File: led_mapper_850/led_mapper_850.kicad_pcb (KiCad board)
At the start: 2 copper layers, 530 parts, among them J1 Conn_02x12_Top_Bottom

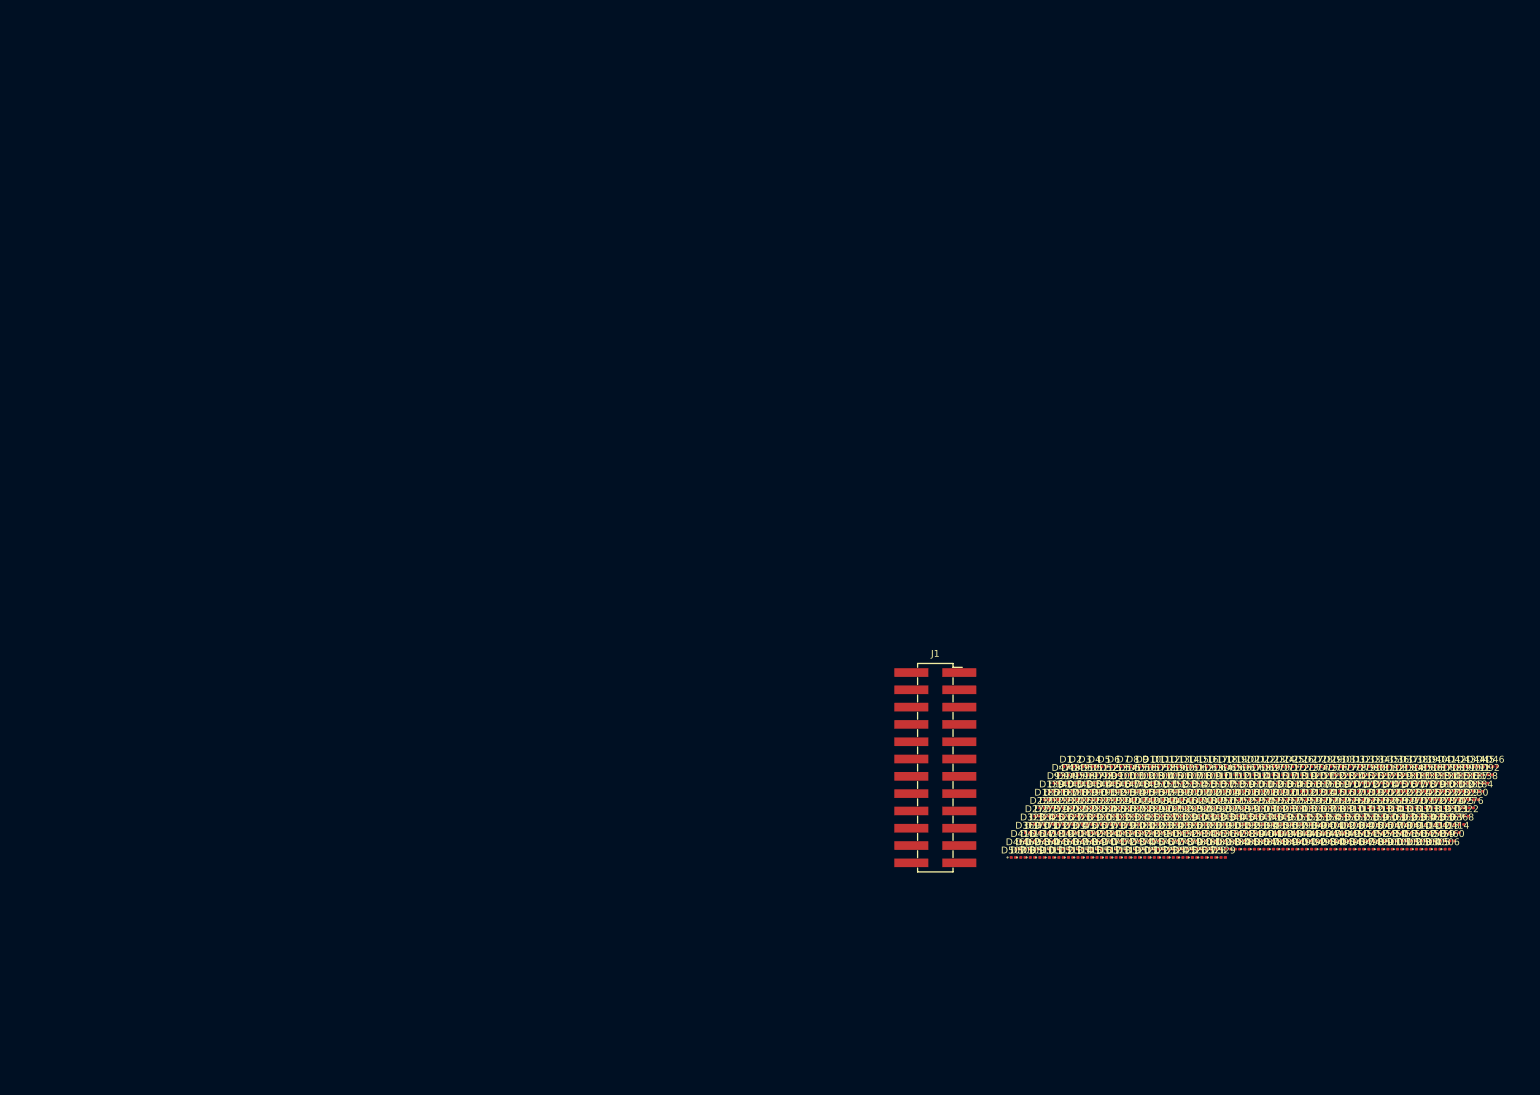
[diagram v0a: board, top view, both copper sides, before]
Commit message: update pcb from schematic
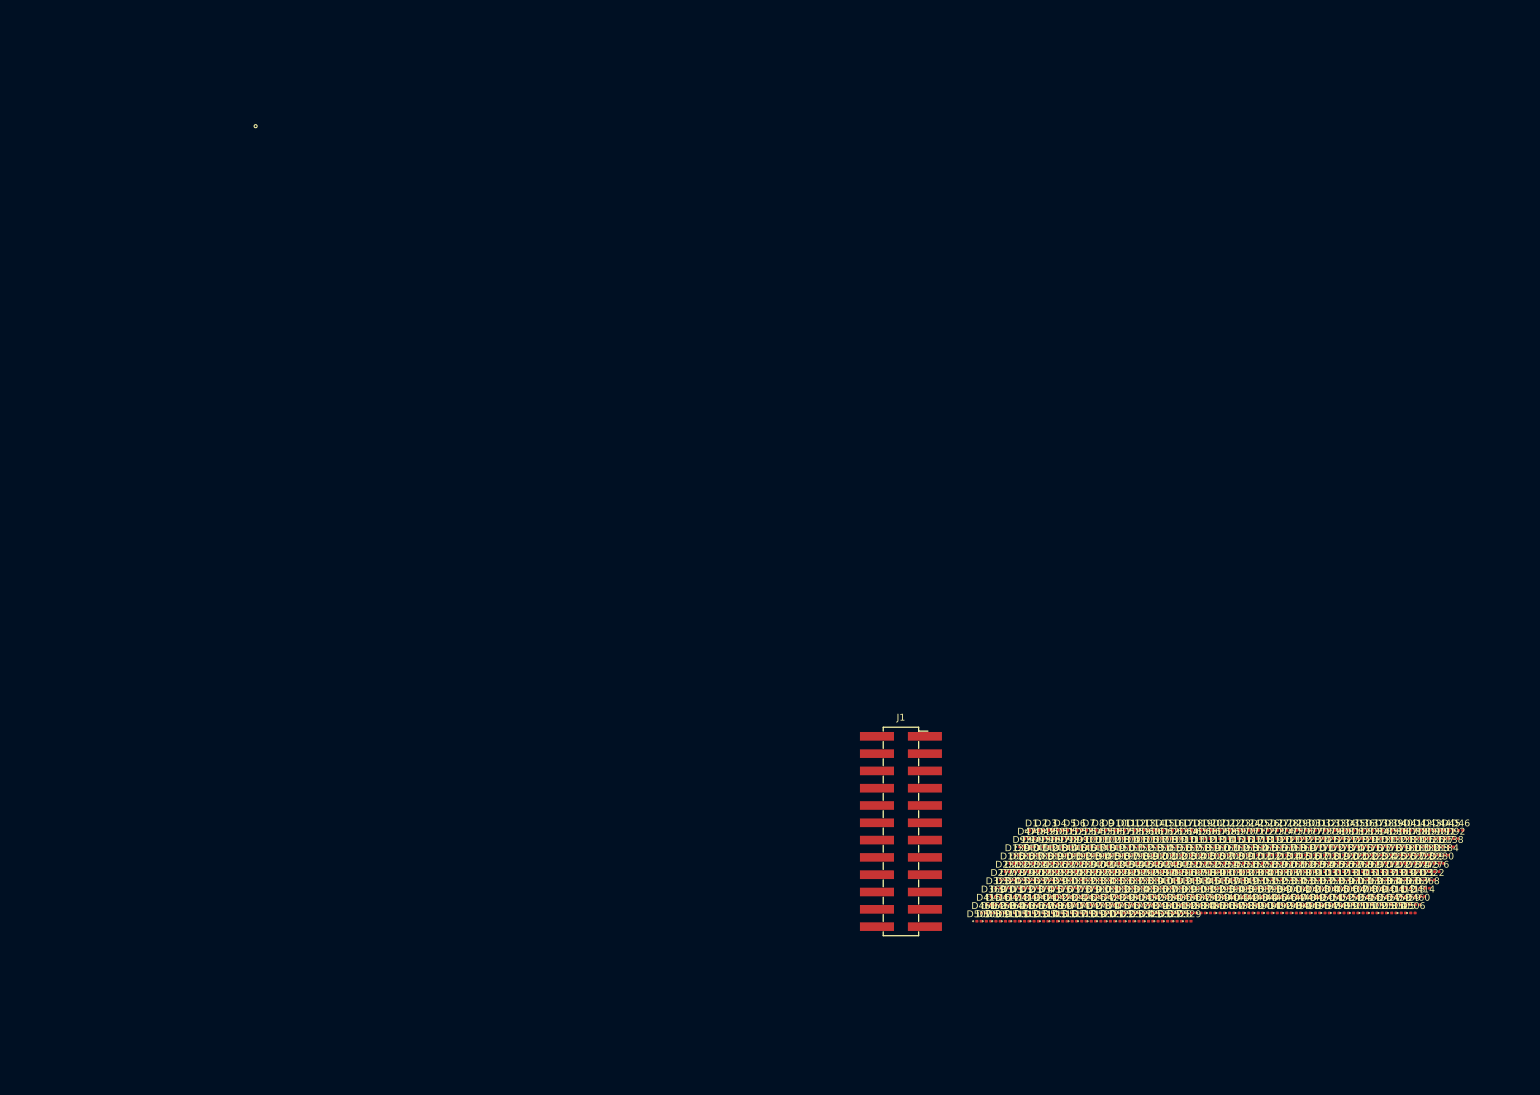
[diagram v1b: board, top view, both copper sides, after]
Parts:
- moved D102 10.6 mm to (125.1, 105.8)
- moved D106 10.6 mm to (130.7, 105.8)
- moved D107 10.6 mm to (132.1, 105.8)
- moved D111 10.6 mm to (137.7, 105.8)
- moved D112 10.6 mm to (139.1, 105.8)
- moved D116 10.6 mm to (144.7, 105.8)
- moved D117 10.6 mm to (146.1, 105.8)
- moved D121 10.6 mm to (151.7, 105.8)
- moved D122 10.6 mm to (153.1, 105.8)
- moved D126 10.6 mm to (158.7, 105.8)
- moved D127 10.6 mm to (160.1, 105.8)
- moved D13 10.6 mm to (130.7, 103.4)
- moved D131 10.6 mm to (165.7, 105.8)
- moved D132 10.6 mm to (167.1, 105.8)
- moved D136 10.6 mm to (172.7, 105.8)
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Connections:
- D151 pad 1: Net-(D151-K) -> /P21
- D152 pad 1: Net-(D151-K) -> /P21
- D153 pad 1: Net-(D151-K) -> /P21
- D154 pad 1: Net-(D151-K) -> /P21
- D155 pad 1: Net-(D151-K) -> /P21
- D156 pad 1: Net-(D151-K) -> /P21
- D157 pad 1: Net-(D151-K) -> /P21
- D158 pad 1: Net-(D151-K) -> /P21
- D159 pad 1: Net-(D151-K) -> /P21
- D160 pad 1: Net-(D151-K) -> /P21
- D161 pad 1: Net-(D151-K) -> /P21
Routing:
- net (no net): vias 0 -> 1

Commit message: place vias
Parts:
- moved J1 28.1 mm to (76.5, 124.9)
- moved D10 8.41 mm to (134.4, 106.3)
- moved D102 8.41 mm to (133.0, 108.7)
- moved D103 8.41 mm to (134.4, 108.7)
- moved D104 8.41 mm to (135.8, 108.7)
- moved D106 8.41 mm to (138.6, 108.7)
- moved D107 8.41 mm to (140.0, 108.7)
- moved D108 8.41 mm to (141.4, 108.7)
- moved D109 8.41 mm to (142.8, 108.7)
- moved D11 8.41 mm to (135.8, 106.3)
- moved D111 8.41 mm to (145.6, 108.7)
- moved D112 8.41 mm to (147.0, 108.7)
- moved D113 8.41 mm to (148.4, 108.7)
- moved D114 8.41 mm to (149.8, 108.7)
- moved D116 8.41 mm to (152.6, 108.7)
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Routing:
- net /P24: vias 0 -> 23
- net /P23: vias 0 -> 23
- net /P22: vias 0 -> 23
- net /P21: vias 0 -> 23
- net /P20: vias 0 -> 23
- net /P19: vias 0 -> 23
- net /P18: vias 0 -> 23
- net /P17: vias 0 -> 23
- net /P16: vias 0 -> 23
- net /P15: vias 0 -> 23
- net /P14: vias 0 -> 23
- net /P13: vias 0 -> 23
- net /P12: vias 0 -> 23
- net /P11: vias 0 -> 23
- net /P10: vias 0 -> 23
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
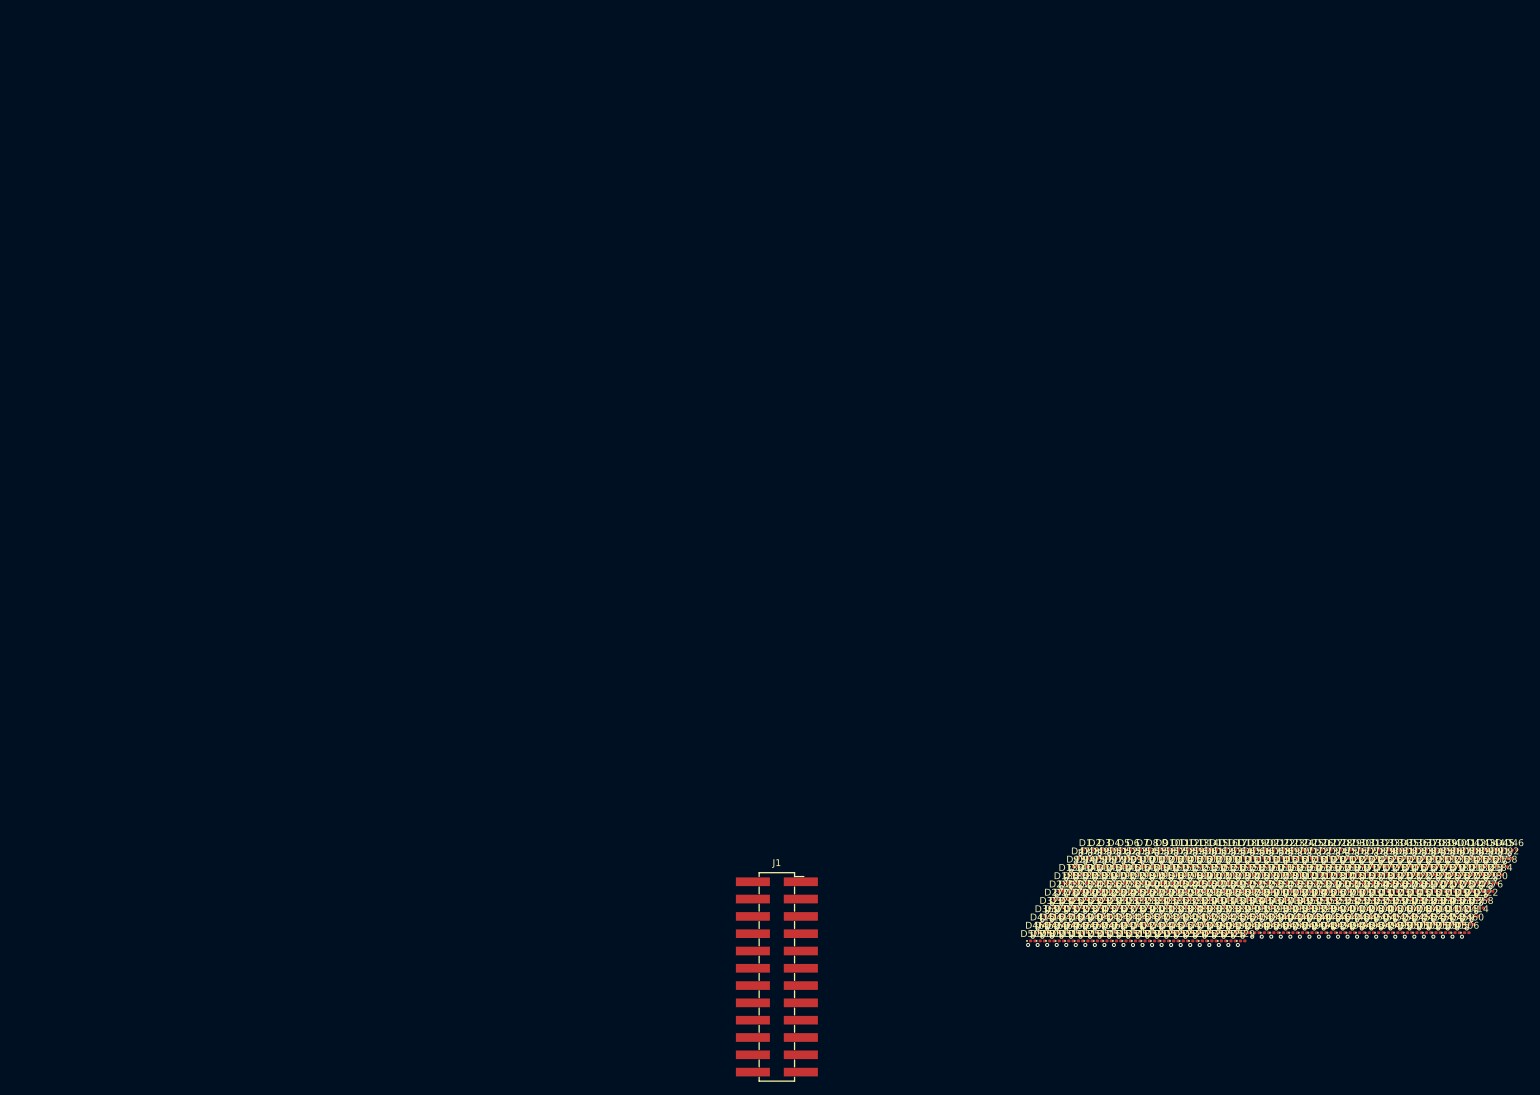
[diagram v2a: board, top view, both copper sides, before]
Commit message: wire most traces
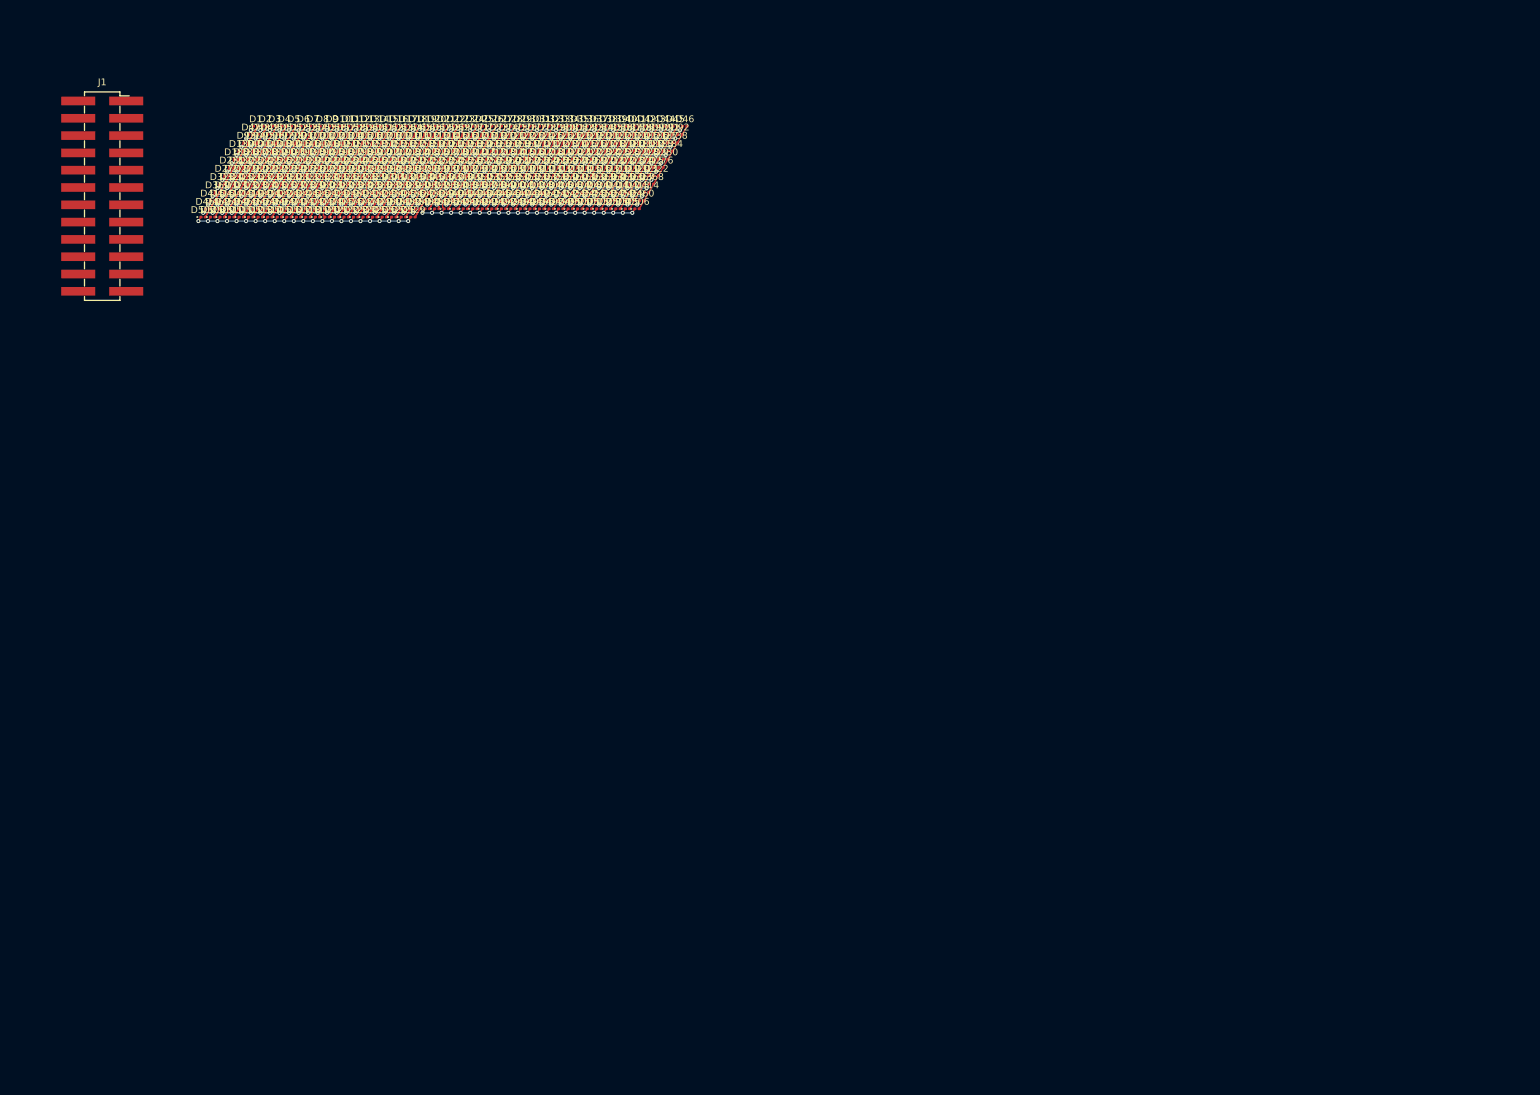
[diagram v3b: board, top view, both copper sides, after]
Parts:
- moved D1 161.6 mm to (0.00, 0.00)
- moved D10 161.6 mm to (12.6, 0.00)
- moved D101 161.6 mm to (9.80, 2.42)
- moved D102 161.6 mm to (11.2, 2.42)
- moved D103 161.6 mm to (12.6, 2.42)
- moved D104 161.6 mm to (14.0, 2.42)
- moved D106 161.6 mm to (16.8, 2.42)
- moved D107 161.6 mm to (18.2, 2.42)
- moved D108 161.6 mm to (19.6, 2.42)
- moved D109 161.6 mm to (21.0, 2.42)
- moved D11 161.6 mm to (14.0, 0.00)
- moved D111 161.6 mm to (23.8, 2.42)
- moved D112 161.6 mm to (25.2, 2.42)
- moved D113 161.6 mm to (26.6, 2.42)
- moved D114 161.6 mm to (28.0, 2.42)
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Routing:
- net /P02: track 0.00 -> 104.4 mm
- net /P03: track 0.00 -> 102.4 mm
- net /P12: track 0.00 -> 91.2 mm
- net /P04: track 0.00 -> 91.2 mm
- net /P11: track 0.00 -> 91.2 mm
- net /P09: track 0.00 -> 91.2 mm
- net /P08: track 0.00 -> 91.2 mm
- net /P07: track 0.00 -> 91.2 mm
- net /P06: track 0.00 -> 91.2 mm
- net /P05: track 0.00 -> 91.2 mm
- net /P10: track 0.00 -> 91.2 mm
- net /P13: track 0.00 -> 90.4 mm
- net /P24: track 0.00 -> 89.8 mm
- net /P18: track 0.00 -> 88.4 mm
- net /P21: track 0.00 -> 88.4 mm
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
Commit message: update remote
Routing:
- net /P17: track 87.0 -> 88.4 mm
- net /P02: track 104.4 -> 103.8 mm
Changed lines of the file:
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@@
+	)
+	(segment
+		(start 18.35 7.641013)
+		(end 18.35 8.257048)
+		(width 0.2)
+		(layer "F.Cu")
+		(net 9)
 	)
 	(segment
@@
 	)
 	(segment
+		(start 18.52 7.471013)
+		(end 18.35 7.641013)
+		(width 0.2)
+		(layer "F.Cu")
+		(net 9)
+	)
+	(segment
 		(start 25.58 8.487048)
 		(end 25.2 9.081266)
@@
 	)
 	(segment
+		(start 18.52 7.274613)
+		(end 18.52 7.471013)
+		(width 0.2)
+		(layer "F.Cu")
+		(net 9)
+	)
+	(segment
 		(start 15.72 9.401266)
 		(end 15.72 9.699484)
@@
 	)
 	(segment
+		(start 18.35 8.257048)
+		(end 18.58 8.487048)
+		(width 0.2)
+		(layer "F.Cu")
+		(net 9)
+	)
+	(segment
 		(start 12.98 8.487048)
 		(end 12.6 9.081266)
@@
 	)
 	(segment
+		(start 24.88 12.540546)
+		(end 24.911556 12.572102)
+		(width 0.2)
+		(layer "F.Cu")
+		(net 14)
+	)
+	(segment
 		(start 1.72 0)
 		(end -5.98 13.336791)
@@
 	)
 	(segment
-		(start 24.88 12.124355)
-		(end 24.5 12.718573)
-		(width 0.2)
-		(layer "F.Cu")
-		(net 14)
-	)
-	(segment
 		(start 27.68 12.124355)
 		(end 27.3 12.718573)
@@
 	)
 	(segment
+		(start 24.88 12.124355)
+		(end 24.88 12.540546)
+		(width 0.2)
+		(layer "F.Cu")
+		(net 14)
+	)
+	(segment
 		(start 33.92 0)
 		(end 27.62 10.91192)
@@
 	)
 	(via
-		(at 24.5 12.718573)
+		(at 24.911556 12.572102)
 		(size 0.6)
 		(drill 0.3)
@@
 	)
 	(segment
-		(start 24.5 12.718573)
-		(end 55.3 12.718573)
+		(start 55.3 12.718573)
+		(end 25.058027 12.718573)
 		(width 0.2)
 		(layer "B.Cu")
+		(net 14)
+	)
+	(segment
+		(start 25.058027 12.718573)
+		(end 24.911556 12.572102)
+		(width 0.2)
+		(layer "B.Cu")
